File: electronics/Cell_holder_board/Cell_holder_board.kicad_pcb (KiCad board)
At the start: 2 copper layers, 101 x 101 mm, 52 parts, among them J1 Conn_01x20_Pin, J2 Load_connector, J3 aux_I, M1 Prototyping_Wood_Hole, M2 Prototyping_Wood_Hole, M3 Prototyping_Wood_Hole, M4 Prototyping_Wood_Hole, Q1 IRLB8721PBF, Q2 IRLB8721PBF, Q3 Q_NMOS_GSD, Q4 Q_NMOS_GSD, Q5 Q_NMOS_GSD, Q6 Q_NMOS_GSD, U1 LTV-817, U10 ACS712xLCTR-20A, U11 LTV-817, U12 LTV-817, U13 LTV-817, U14 LTV-817, U2 1043P, U3 1043P, U4 1043P, U5 1043P

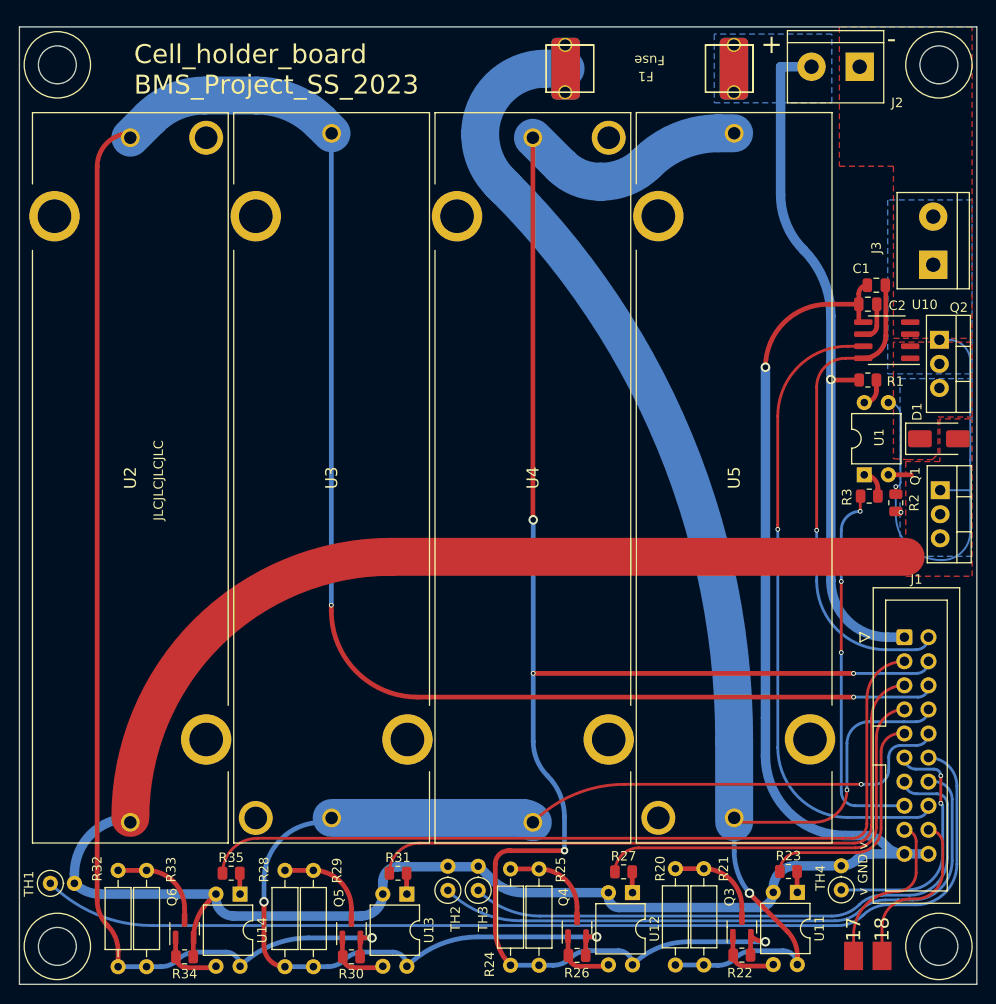
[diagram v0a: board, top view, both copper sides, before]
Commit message: finalized cell_board_holder
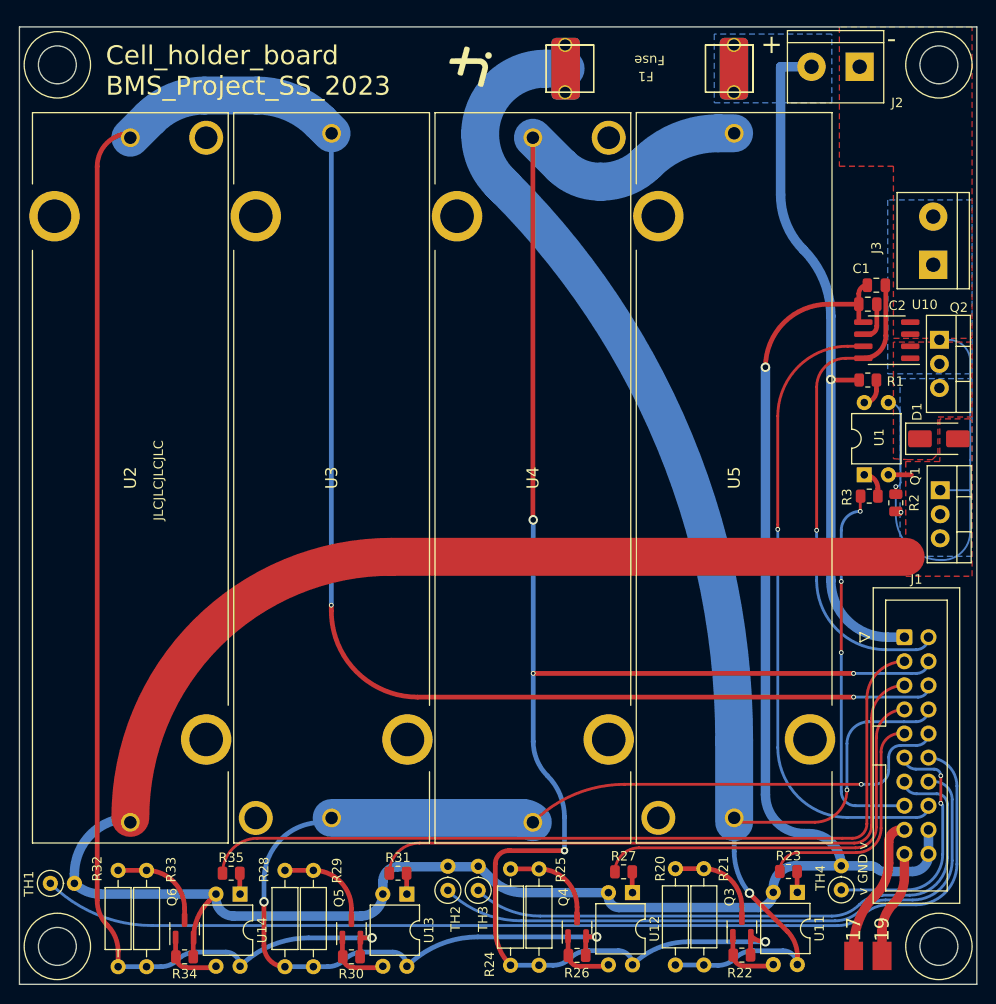
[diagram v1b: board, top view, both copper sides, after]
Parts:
- added G***: LOGO, BMS_lib:thi_logo_original, F.Cu at (98.6, 63.2)
- added G***: LOGO, BMS_lib:thi_logo_large, B.Cu at (101.6, 103.5)
- PAD2: value 18 -> 19
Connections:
- J1 pad 18: Net-(J1-Pin_18) -> GND
- J1 pad 19: GND -> Net-(J1-Pin_19)
- PAD2 pad 1: Net-(J1-Pin_18) -> Net-(J1-Pin_19)
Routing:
- net Net-(J1-Pin_18): track 17.8 -> 0.00 mm
- net Net-(J1-Pin_19): track 0.00 -> 11.4 mm
- net Net-(J1-Pin_17): track 17.5 -> 15.3 mm

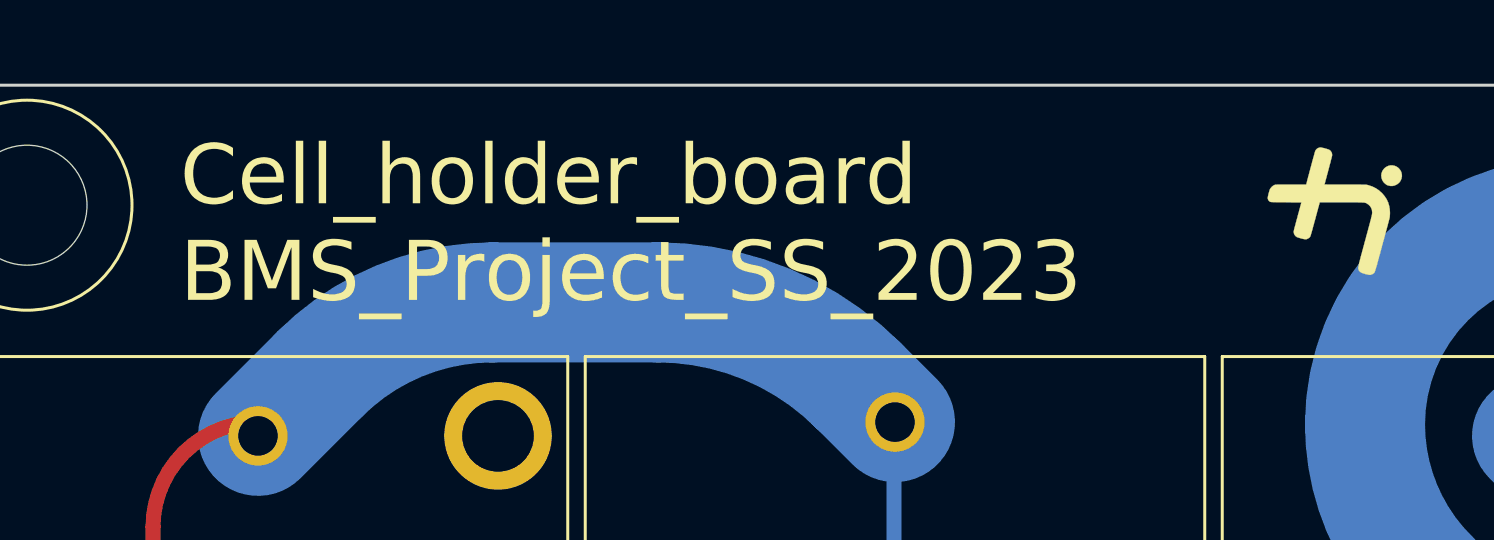
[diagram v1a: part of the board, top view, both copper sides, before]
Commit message: Finished layout of main board and finalized lyout of cell board (added names & THI logo), changed pinout of tray plug
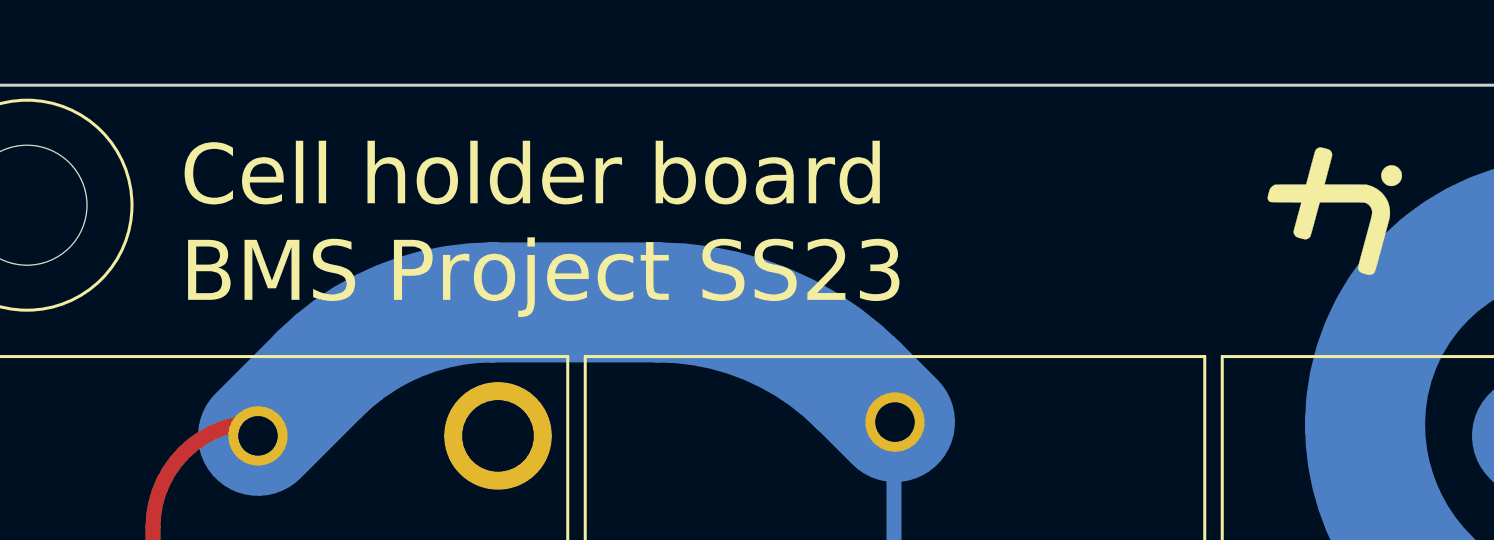
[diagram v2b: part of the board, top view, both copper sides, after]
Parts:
- moved G*** 12.2 mm to (113.8, 103.3)
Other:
- board text added: "Cell holder board BMS Project SS23"
- board text added: "Tjorven Hillmann Wilken Hemme Henry Pasch Michael Witti Jonathan Böke Fabian Mast Gina-Madeleine Haase A. Furkan Can Ramón Fürst"
- board text removed: "Cell_holder_board BMS_Project_SS_2023"
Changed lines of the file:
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@@
   )
   (footprint "BMS_lib:thi_logo_large" (layer "B.Cu")
-    (at 101.6 103.5 180)
+    (at 113.8 103.3 180)
     (attr through_hole)
     (fp_text reference "G***" (at 0 0) (layer "B.SilkS") hide
@@
   (gr_rect (start 51 59) (end 152 160)
     (stroke (width 0.1) (type default)) (fill none) (layer "Edge.Cuts"))
-  (gr_text "Cell_holder_board\nBMS_Project_SS_2023" (at 60.1 66.4) (layer "F.SilkS")
+  (gr_text "Tjorven Hillmann\nWilken Hemme\nHenry Pasch\nMichael Witti\nJonathan Böke\nFabian Mast\nGina-Madeleine Haase\nA. Furkan Can\nRamón Fürst" (at 93 120.7) (layer "B.SilkS")
+    (effects (font (size 2 2) (thickness 0.3)) (justify left bottom mirror))
+  )
+  (gr_text "Cell holder board\nBMS Project SS23" (at 60.1 66.4) (layer "F.SilkS")
     (effects (font (size 2 2) (thickness 0.3)) (justify left bottom))
   )

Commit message: exported PCB's as gerber files
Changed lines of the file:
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@@
       (plot_on_all_layers_selection 0x0000000_00000000)
       (disableapertmacros false)
-      (usegerberextensions false)
-      (usegerberattributes true)
-      (usegerberadvancedattributes true)
-      (creategerberjobfile true)
+      (usegerberextensions true)
+      (usegerberattributes false)
+      (usegerberadvancedattributes false)
+      (creategerberjobfile false)
       (dashed_line_dash_ratio 12.000000)
       (dashed_line_gap_ratio 3.000000)
@@
       (plotinvisibletext false)
       (sketchpadsonfab false)
-      (subtractmaskfromsilk false)
+      (subtractmaskfromsilk true)
       (outputformat 1)
       (mirror false)
-      (drillshape 1)
+      (drillshape 0)
       (scaleselection 1)
       (outputdirectory "")
@@
     (fp_line (start 1 0.625) (end -1 0.625)
       (stroke (width 0.1) (type solid)) (layer "F.Fab"))
-    (pad "1" smd roundrect (at -0.9125 0) (size 1.025 1.4) (layers "F.Cu" "F.Paste" "F.Mask") (roundrect_rratio 0.243902)
+    (pad "1" smd roundrect (at -0.9125 0) (size 1.025 1.4) (layers "F.Cu" "F.Paste" "F.Mask") (roundrect_rratio 0.243902439)
       (net 9 "/balancing_ctrl_4") (pintype "passive"))
-    (pad "2" smd roundrect (at 0.9125 0) (size 1.025 1.4) (layers "F.Cu" "F.Paste" "F.Mask") (roundrect_rratio 0.243902)
+    (pad "2" smd roundrect (at 0.9125 0) (size 1.025 1.4) (layers "F.Cu" "F.Paste" "F.Mask") (roundrect_rratio 0.243902439)
       (net 34 "Net-(R23-Pad2)") (pintype "passive"))
     (model "${KICAD6_3DMODEL_DIR}/Resistor_SMD.3dshapes/R_0805_2012Metric.wrl"
@@
     (fp_line (start 1 0.625) (end -1 0.625)
       (stroke (width 0.1) (type solid)) (layer "F.Fab"))
-    (pad "1" smd roundrect (at -0.9125 0) (size 1.025 1.4) (layers "F.Cu" "F.Paste" "F.Mask") (roundrect_rratio 0.243902)
+    (pad "1" smd roundrect (at -0.9125 0) (size 1.025 1.4) (layers "F.Cu" "F.Paste" "F.Mask") (roundrect_rratio 0.243902439)
       (net 8 "/balancing_ctrl_3") (pintype "passive"))
-    (pad "2" smd roundrect (at 0.9125 0) (size 1.025 1.4) (layers "F.Cu" "F.Paste" "F.Mask") (roundrect_rratio 0.243902)
+    (pad "2" smd roundrect (at 0.9125 0) (size 1.025 1.4) (layers "F.Cu" "F.Paste" "F.Mask") (roundrect_rratio 0.243902439)
       (net 35 "Net-(R27-Pad2)") (pintype "passive"))
     (model "${KICAD6_3DMODEL_DIR}/Resistor_SMD.3dshapes/R_0805_2012Metric.wrl"
@@
     (fp_line (start 1 0.625) (end -1 0.625)
       (stroke (width 0.1) (type solid)) (layer "F.Fab"))
-    (pad "1" smd roundrect (at -0.9125 0) (size 1.025 1.4) (layers "F.Cu" "F.Paste" "F.Mask") (roundrect_rratio 0.243902)
+    (pad "1" smd roundrect (at -0.9125 0) (size 1.025 1.4) (layers "F.Cu" "F.Paste" "F.Mask") (roundrect_rratio 0.243902439)
       (net 5 "+BATT") (pintype "passive"))
-    (pad "2" smd roundrect (at 0.9125 0) (size 1.025 1.4) (layers "F.Cu" "F.Paste" "F.Mask") (roundrect_rratio 0.243902)
+    (pad "2" smd roundrect (at 0.9125 0) (size 1.025 1.4) (layers "F.Cu" "F.Paste" "F.Mask") (roundrect_rratio 0.243902439)
       (net 32 "Net-(R1-Pad2)") (pintype "passive"))
     (model "${KICAD6_3DMODEL_DIR}/Resistor_SMD.3dshapes/R_0805_2012Metric.wrl"
@@
     (fp_line (start 1 0.625) (end -1 0.625)
       (stroke (width 0.1) (type solid)) (layer "F.Fab"))
-    (pad "1" smd roundrect (at -0.9125 0) (size 1.025 1.4) (layers "F.Cu" "F.Paste" "F.Mask") (roundrect_rratio 0.243902)
+    (pad "1" smd roundrect (at -0.9125 0) (size 1.025 1.4) (layers "F.Cu" "F.Paste" "F.Mask") (roundrect_rratio 0.243902439)
       (net 24 "Net-(Q3-G)") (pintype "passive"))
-    (pad "2" smd roundrect (at 0.9125 0) (size 1.025 1.4) (layers "F.Cu" "F.Paste" "F.Mask") (roundrect_rratio 0.243902)
+    (pad "2" smd roundrect (at 0.9125 0) (size 1.025 1.4) (layers "F.Cu" "F.Paste" "F.Mask") (roundrect_rratio 0.243902439)
       (net 12 "/bat03") (pintype "passive"))
     (model "${KICAD6_3DMODEL_DIR}/Resistor_SMD.3dshapes/R_0805_2012Metric.wrl"
@@
     (fp_line (start 1 0.625) (end -1 0.625)
       (stroke (width 0.1) (type solid)) (layer "F.Fab"))
-    (pad "1" smd roundrect (at -0.9125 0) (size 1.025 1.4) (layers "F.Cu" "F.Paste" "F.Mask") (roundrect_rratio 0.243902)
+    (pad "1" smd roundrect (at -0.9125 0) (size 1.025 1.4) (layers "F.Cu" "F.Paste" "F.Mask") (roundrect_rratio 0.243902439)
       (net 17 "/bat_main_switch") (pintype "passive"))
-    (pad "2" smd roundrect (at 0.9125 0) (size 1.025 1.4) (layers "F.Cu" "F.Paste" "F.Mask") (roundrect_rratio 0.243902)
+    (pad "2" smd roundrect (at 0.9125 0) (size 1.025 1.4) (layers "F.Cu" "F.Paste" "F.Mask") (roundrect_rratio 0.243902439)
       (net 33 "Net-(R3-Pad2)") (pintype "passive"))
     (model "${KICAD6_3DMODEL_DIR}/Resistor_SMD.3dshapes/R_0805_2012Metric.wrl"
@@
     (fp_line (start 1 0.625) (end -1 0.625)
       (stroke (width 0.1) (type solid)) (layer "F.Fab"))
-    (pad "1" smd roundrect (at -0.9125 0) (size 1.025 1.4) (layers "F.Cu" "F.Paste" "F.Mask") (roundrect_rratio 0.243902)
+    (pad "1" smd roundrect (at -0.9125 0) (size 1.025 1.4) (layers "F.Cu" "F.Paste" "F.Mask") (roundrect_rratio 0.243902439)
       (net 6 "/balancing_ctrl_1") (pintype "passive"))
-    (pad "2" smd roundrect (at 0.9125 0) (size 1.025 1.4) (layers "F.Cu" "F.Paste" "F.Mask") (roundrect_rratio 0.243902)
+    (pad "2" smd roundrect (at 0.9125 0) (size 1.025 1.4) (layers "F.Cu" "F.Paste" "F.Mask") (roundrect_rratio 0.243902439)
       (net 37 "Net-(R35-Pad2)") (pintype "passive"))
     (model "${KICAD6_3DMODEL_DIR}/Resistor_SMD.3dshapes/R_0805_2012Metric.wrl"
@@
     (fp_line (start 5.72 27.96) (end -3.18 27.96)
       (stroke (width 0.1) (type solid)) (layer "F.Fab"))
-    (pad "1" thru_hole roundrect (at 0 0) (size 1.7 1.7) (drill 1) (layers "*.Cu" "*.Mask") (roundrect_rratio 0.147059)
+    (pad "1" thru_hole roundrect (at 0 0) (size 1.7 1.7) (drill 1) (layers "*.Cu" "*.Mask") (roundrect_rratio 0.1470588235)
       (net 5 "+BATT") (pinfunction "Pin_1") (pintype "passive"))
     (pad "2" thru_hole circle (at 2.54 0) (size 1.7 1.7) (drill 1) (layers "*.Cu" "*.Mask")
@@
     (fp_line (start 1 0.625) (end -1 0.625)
       (stroke (width 0.1) (type solid)) (layer "F.Fab"))
-    (pad "1" smd roundrect (at -0.9125 0 270) (size 1.025 1.4) (layers "F.Cu" "F.Paste" "F.Mask") (roundrect_rratio 0.243902)
+    (pad "1" smd roundrect (at -0.9125 0 270) (size 1.025 1.4) (layers "F.Cu" "F.Paste" "F.Mask") (roundrect_rratio 0.243902439)
       (net 22 "Net-(Q1-G)") (pintype "passive"))
-    (pad "2" smd roundrect (at 0.9125 0 270) (size 1.025 1.4) (layers "F.Cu" "F.Paste" "F.Mask") (roundrect_rratio 0.243902)
+    (pad "2" smd roundrect (at 0.9125 0 270) (size 1.025 1.4) (layers "F.Cu" "F.Paste" "F.Mask") (roundrect_rratio 0.243902439)
       (net 23 "Net-(Q1-S)") (pintype "passive"))
     (model "${KICAD6_3DMODEL_DIR}/Resistor_SMD.3dshapes/R_0805_2012Metric.wrl"
@@
     (fp_line (start 1 0.625) (end -1 0.625)
       (stroke (width 0.1) (type solid)) (layer "F.Fab"))
-    (pad "1" smd roundrect (at -0.9125 0) (size 1.025 1.4) (layers "F.Cu" "F.Paste" "F.Mask") (roundrect_rratio 0.243902)
+    (pad "1" smd roundrect (at -0.9125 0) (size 1.025 1.4) (layers "F.Cu" "F.Paste" "F.Mask") (roundrect_rratio 0.243902439)
       (net 30 "Net-(Q6-G)") (pintype "passive"))
-    (pad "2" smd roundrect (at 0.9125 0) (size 1.025 1.4) (layers "F.Cu" "F.Paste" "F.Mask") (roundrect_rratio 0.243902)
+    (pad "2" smd roundrect (at 0.9125 0) (size 1.025 1.4) (layers "F.Cu" "F.Paste" "F.Mask") (roundrect_rratio 0.243902439)
       (net 2 "GND") (pintype "passive"))
     (model "${KICAD6_3DMODEL_DIR}/Resistor_SMD.3dshapes/R_0805_2012Metric.wrl"
@@
     (fp_line (start 1 0.625) (end -1 0.625)
       (stroke (width 0.1) (type solid)) (layer "F.Fab"))
-    (pad "1" smd roundrect (at -0.9125 0) (size 1.025 1.4) (layers "F.Cu" "F.Paste" "F.Mask") (roundrect_rratio 0.243902)
+    (pad "1" smd roundrect (at -0.9125 0) (size 1.025 1.4) (layers "F.Cu" "F.Paste" "F.Mask") (roundrect_rratio 0.243902439)
       (net 7 "/balancing_ctrl_2") (pintype "passive"))
-    (pad "2" smd roundrect (at 0.9125 0) (size 1.025 1.4) (layers "F.Cu" "F.Paste" "F.Mask") (roundrect_rratio 0.243902)
+    (pad "2" smd roundrect (at 0.9125 0) (size 1.025 1.4) (layers "F.Cu" "F.Paste" "F.Mask") (roundrect_rratio 0.243902439)
       (net 36 "Net-(R31-Pad2)") (pintype "passive"))
     (model "${KICAD6_3DMODEL_DIR}/Resistor_SMD.3dshapes/R_0805_2012Metric.wrl"
@@
     (fp_line (start 1 0.625) (end -1 0.625)
       (stroke (width 0.1) (type solid)) (layer "F.Fab"))
-    (pad "1" smd roundrect (at -0.9125 0) (size 1.025 1.4) (layers "F.Cu" "F.Paste" "F.Mask") (roundrect_rratio 0.243902)
+    (pad "1" smd roundrect (at -0.9125 0) (size 1.025 1.4) (layers "F.Cu" "F.Paste" "F.Mask") (roundrect_rratio 0.243902439)
       (net 26 "Net-(Q4-G)") (pintype "passive"))
-    (pad "2" smd roundrect (at 0.9125 0) (size 1.025 1.4) (layers "F.Cu" "F.Paste" "F.Mask") (roundrect_rratio 0.243902)
+    (pad "2" smd roundrect (at 0.9125 0) (size 1.025 1.4) (layers "F.Cu" "F.Paste" "F.Mask") (roundrect_rratio 0.243902439)
       (net 11 "/bat02") (pintype "passive"))
     (model "${KICAD6_3DMODEL_DIR}/Resistor_SMD.3dshapes/R_0805_2012Metric.wrl"
@@
     (fp_line (start 1 0.625) (end -1 0.625)
       (stroke (width 0.1) (type solid)) (layer "F.Fab"))
-    (pad "1" smd roundrect (at -0.9125 0) (size 1.025 1.4) (layers "F.Cu" "F.Paste" "F.Mask") (roundrect_rratio 0.243902)
+    (pad "1" smd roundrect (at -0.9125 0) (size 1.025 1.4) (layers "F.Cu" "F.Paste" "F.Mask") (roundrect_rratio 0.243902439)
       (net 28 "Net-(Q5-G)") (pintype "passive"))
-    (pad "2" smd roundrect (at 0.9125 0) (size 1.025 1.4) (layers "F.Cu" "F.Paste" "F.Mask") (roundrect_rratio 0.243902)
+    (pad "2" smd roundrect (at 0.9125 0) (size 1.025 1.4) (layers "F.Cu" "F.Paste" "F.Mask") (roundrect_rratio 0.243902439)
       (net 10 "/bat01") (pintype "passive"))
     (model "${KICAD6_3DMODEL_DIR}/Resistor_SMD.3dshapes/R_0805_2012Metric.wrl"
